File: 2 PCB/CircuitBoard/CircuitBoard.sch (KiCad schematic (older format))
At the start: 49 parts, among them J1 Conn_01x04_Male, J10 Conn_01x04_Male, J11 Conn_01x04_Male, J12 Conn_01x04_Male, J13 Conn_01x04_Male, J14 Conn_01x04_Male, J15 Conn_01x04_Male, J16 Conn_01x04_Male, J17 Conn_01x04_Male, J18 Conn_01x04_Male, J19 Conn_01x04_Male, J2 Conn_01x04_Male, J20 Conn_01x04_Male, J21 Conn_01x24_Female, J22 Conn_01x24_Female, J23 Conn_01x04_Male, J24 Conn_01x04_Male, J25 Conn_01x04_Male, J26 Conn_01x04_Male, J27 Conn_01x04_Male, J28 Conn_01x04_Male, J29 Conn_01x04_Male, J3 Conn_01x04_Male, J30 Conn_01x04_Male, J31 Conn_01x04_Male, J32 Conn_01x04_Male, J33 Conn_01x04_Male, J34 Conn_01x04_Male, J35 Conn_01x04_Male, J36 Conn_01x04_Male, J37 Conn_01x04_Male, J38 Conn_01x04_Male, J39 Conn_01x04_Male, J4 Conn_01x04_Male, J40 Conn_01x04_Male, J41 Conn_01x04_Male, J42 Conn_01x04_Male, J5 Conn_01x04_Male, J6 Conn_01x04_Male, J7 Conn_01x04_Male, J8 Conn_01x04_Male, J9 Conn_01x04_Male, U1 TXS0108EPWR, U2 TXS0108EPWR, U3 TXS0108EPWR, U4 TXS0108EPWR, U5 TXS0108EPWR

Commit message: Production PCB Added
Production PCB Added it was noticed since prodution there is an issue with the PCB that needs to be addressed in a future update. For now it can be fixed mostly by ripping the resistor off the board. Ideally then a wire will be soldered in its place to 3.3V
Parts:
- R1: footprint Resistor_SMD:R_0201_0603Metric -> Resistor_SMD:R_0603_1608Metric
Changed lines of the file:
@@
 F 0 "R1" H 3870 1096 50  0000 L CNN
 F 1 "10k" H 3870 1005 50  0000 L CNN
-F 2 "Resistor_SMD:R_0201_0603Metric" V 3730 1050 50  0001 C CNN
+F 2 "Resistor_SMD:R_0603_1608Metric" V 3730 1050 50  0001 C CNN
 F 3 "~" H 3800 1050 50  0001 C CNN
 	1    3800 1050

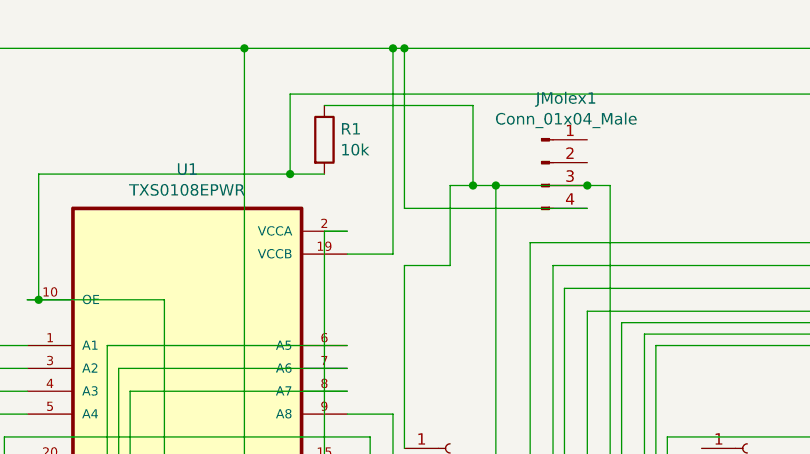
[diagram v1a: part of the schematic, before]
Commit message: PCB V2 & Case Work & Code Updates
PCB Version 2 started and completed. This makes it smaller and should fix the issues with having to solder a patch wire to the board. It also makes pin 13 no longer used for controlling the connected RGB components as it should not glow constantly which could disrupt RGB patterns. The new PCB also uses a much better mounting system for the Molex power connector. It also increased the trace width for the power traces to increase the current capabilities. As well a new case was started for covering the PCB inside a computer. Lastly, the Default pattern was bug fixed to no longer have issues with the MAXPIXELS constant being under 255. It also reflects the PCB change for pin 13.
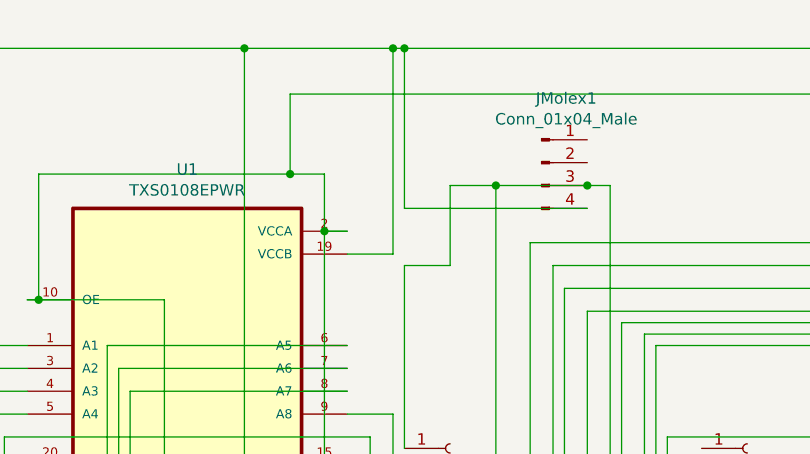
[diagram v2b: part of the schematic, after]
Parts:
- removed R1: 10k, Resistor_SMD:R_0603_1608Metric, symbol Device:R
- JMolex1: footprint Connector_TE-Connectivity:TE_MATE-N-LOK_350211-1_1x04_P5.08mm_Vertical -> Molex:7708461
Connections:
- net at J21.15 (Pin_15), U1.2 (VCCA), U2.2 (VCCA)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: now also U1.10 (OE), U2.10 (OE), U3.10 (OE), U4.10 (OE), U5.10 (OE)
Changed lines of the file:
@@
 F 0 "JMolex1" H 4858 1431 50  0000 C CNN
 F 1 "Conn_01x04_Male" H 4858 1340 50  0000 C CNN
-F 2 "Connector_TE-Connectivity:TE_MATE-N-LOK_350211-1_1x04_P5.08mm_Vertical" H 4750 1150 50  0001 C CNN
+F 2 "Molex:7708461" H 4750 1150 50  0001 C CNN
 F 3 "~" H 4750 1150 50  0001 C CNN
 	1    4750 1150
@@
 	4100 2250 3900 2250
 Wire Wire Line
-	3900 3700 3900 3900
-Wire Wire Line
 	3550 3600 3550 4200
 Wire Wire Line
@@
 Wire Wire Line
 	4350 6250 3900 6250
-Wire Wire Line
-	4150 3700 3900 3700
 Wire Wire Line
 	4150 3600 3550 3600
@@
 Wire Wire Line
 	4350 1600 4350 1250
-Wire Wire Line
-	4350 1250 4450 1250
 Connection ~ 4550 1250
-$Comp
-L Device:R R1
-U 1 1 61B41D15
-P 3800 1050
-F 0 "R1" H 3870 1096 50  0000 L CNN
-F 1 "10k" H 3870 1005 50  0000 L CNN
-F 2 "Resistor_SMD:R_0603_1608Metric" V 3730 1050 50  0001 C CNN
-F 3 "~" H 3800 1050 50  0001 C CNN
-	1    3800 1050
-	1    0    0    -1
-$EndComp
 Wire Wire Line
 	2550 1200 2550 1750
 Wire Wire Line
 	2550 1750 2500 1750
-Wire Wire Line
-	3800 900  4450 900
-Wire Wire Line
-	4450 900  4450 1250
-Connection ~ 4450 1250
-Wire Wire Line
-	4450 1250 4550 1250
 Wire Wire Line
 	2550 1750 3100 1750
@@
 Connection ~ 3650 1200
 Wire Wire Line
-	3650 1200 3800 1200
-Wire Wire Line
 	6250 850  6250 3250
 Wire Wire Line
@@
 Wire Wire Line
 	9750 2800 9750 2950
+Wire Wire Line
+	3650 1200 3800 1200
+Wire Wire Line
+	4350 1250 4550 1250
+Wire Wire Line
+	4150 3700 3900 3700
+Wire Wire Line
+	3900 3700 3900 3900
+Wire Wire Line
+	3800 1450 3800 1200
+Connection ~ 3800 1450
 $EndSCHEMATC
